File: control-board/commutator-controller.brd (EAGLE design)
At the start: 43 x 95 mm, 41 parts, among them U1 PTN04050C, U2 LTC4425EMSE#PBF, U3 IS31FL3193, U4 TMC2130, U5 TEENSY_LC

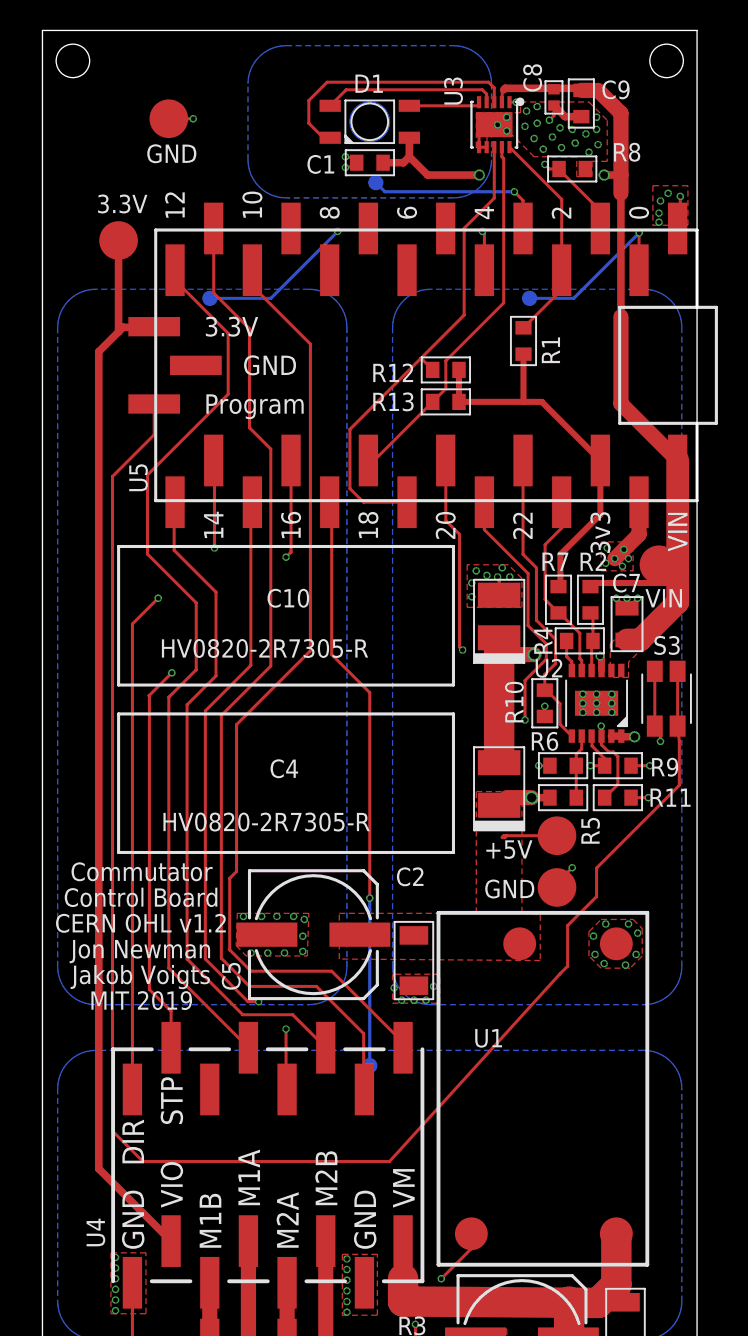
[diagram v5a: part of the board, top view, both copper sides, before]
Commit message: Updates to README, firmware, and control-board
- Fixed mirrored pads for super capacitor charger
- Switched Teensy LC for Teensy 3.2
- Moved Teensy in 2mm so that housing does not need large cutout, but
small one for micro USB
- Fixed other small issues with the circuit
- Some small changed to firmware: speed now provided directly in RPM
instead of scale factor. Boundary checks on values. Some other things
too.
- Updated README
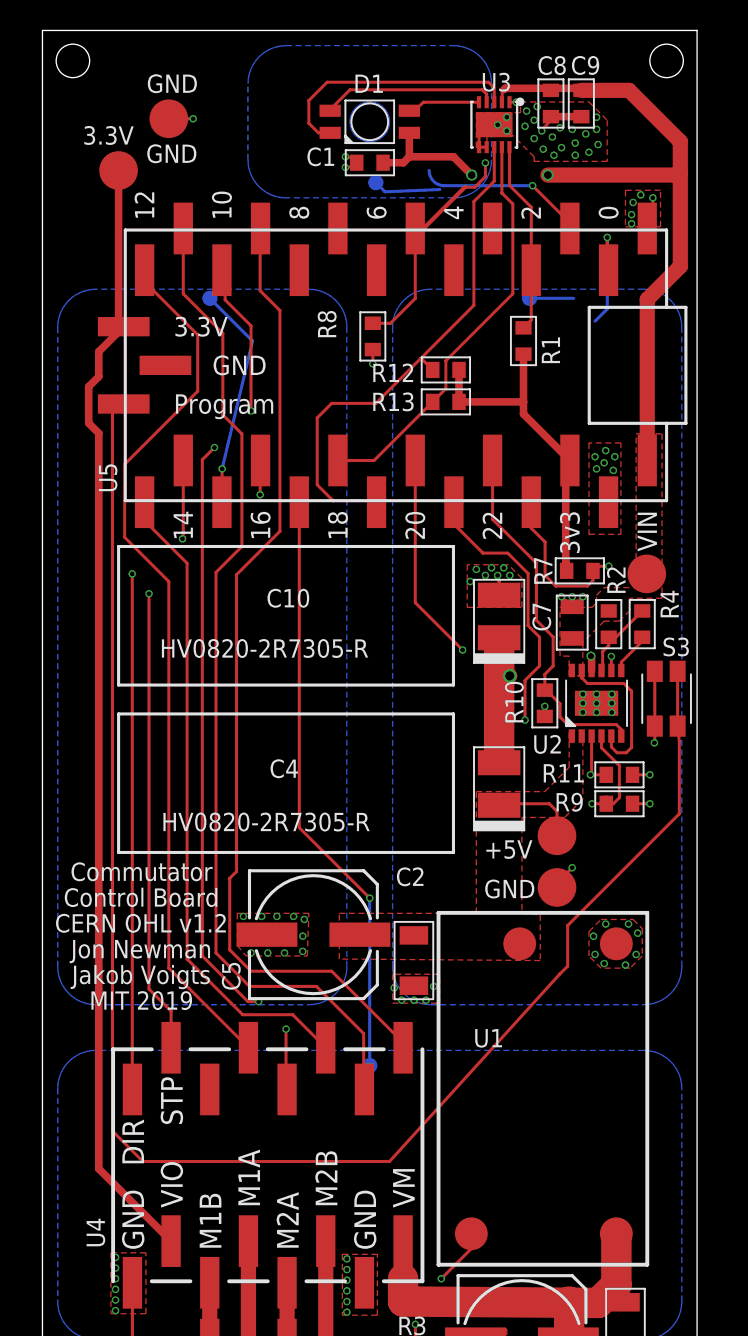
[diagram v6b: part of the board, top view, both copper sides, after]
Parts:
- removed R5: 0, jonnew:0603
- removed R6: DNP, jonnew:0603
- C8: device jonnew:0402 -> jonnew:0603
- S3: value (none) -> EVQP7J
- U5: value TEENSY_LC -> TEENSY-3.2
- moved R8 17.1 mm to (21.7, 74.9), turned to 270 degrees
- moved +3.3V 4.60 mm to (5.00, 85.8)
- moved R4 4.24 mm to (39.4, 56.0), turned to 90 degrees
- moved C7 3.60 mm to (34.8, 56.1)
- moved R9 2.50 mm to (37.9, 44.2)
- moved R7 2.36 mm to (35.3, 59.5), turned to 180 degrees
- moved R2 2.00 mm to (37.2, 56.0)
- moved U5 2.00 mm to (41.0, 73.0)
- moved R11 1.50 mm to (37.9, 46.1)
- moved +5V1 1.00 mm to (39.7, 59.3)
- moved C8 0.45 mm to (33.4, 90.2)
- turned U2 to 90 degrees
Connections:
- removed net N$4: R5.1, R6.2, U2.5
- net !IS31_SHDN: now also U5.5; no longer U5.1
- net +5V0: no longer R5.2
- net CCW: now also U5.15; no longer U5.4
- net CFG-3/!TMC_CS: now also U5.10; no longer U5.15
- net GND: no longer R6.1
- net MODE: now also U5.1; no longer U5.3
- net TMC_EN: now also U5.9; no longer U5.10
- net VCC: now also U2.5
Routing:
- net CFG-3/!TMC_CS: track 42.5 -> 60.2 mm, vias 2 -> 4
- net !IS31_SHDN: track 11.5 -> 25.7 mm
- net +5V0: track 19.0 -> 6.35 mm, vias 2 -> 0
- net CCW: track 22.3 -> 14.8 mm, vias 2 -> 1
- net VMID_SEL: track 28.6 -> 34.6 mm
- net !PFO: track 12.5 -> 17.6 mm, vias 0 -> 2
- net N$4: track 4.19 -> 0.00 mm
- net MOT_POW_EN: track 20.1 -> 24.0 mm
- net DIR: track 47.2 -> 43.3 mm
- net GND: track 38.6 -> 34.7 mm, vias 105 -> 107
- net MODE: track 12.0 -> 15.5 mm
- net SCL: track 31.7 -> 34.3 mm
- net SDA: track 24.5 -> 27.0 mm
- net V_BM: track 14.3 -> 12.7 mm
- net VCC: track 72.3 -> 73.8 mm
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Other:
- board text added: "Commutator v1.1 OHL v1.2"
- board text removed: "Commutator v1.0 OHL v1.2"
- board text removed: "VIN"
